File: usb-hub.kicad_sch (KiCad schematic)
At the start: 17 parts, among them U5 CH334P, Y2 X322512MSB4SI

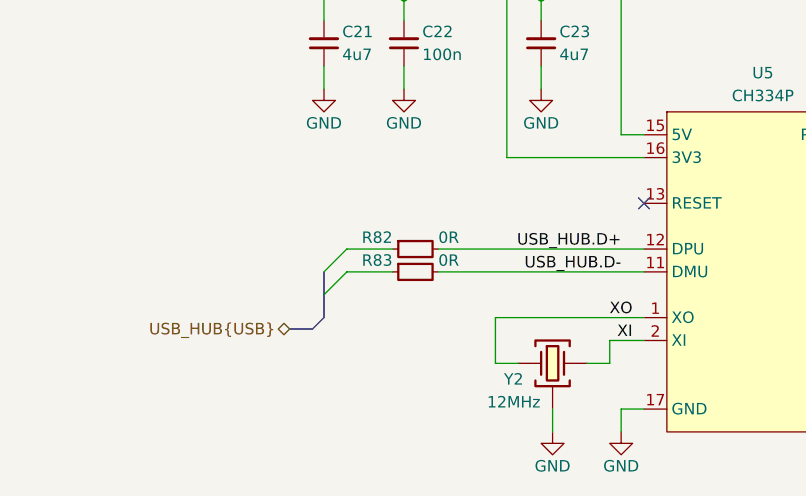
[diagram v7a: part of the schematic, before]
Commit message: [#3] Continue layout, minor schematic fixes, add power switch for CAN transceiver 5V rail
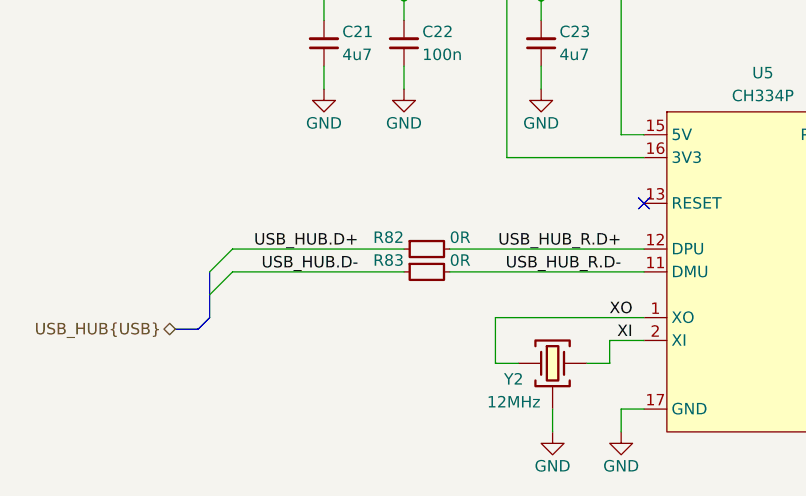
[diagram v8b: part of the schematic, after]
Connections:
- net USB_HUB.D+: now also R82.1; no longer R82.2, U5.12 (DPU)
- net USB_HUB.D-: now also R83.1; no longer R83.2, U5.11 (DMU)
- new net USB_HUB_R.D+: R82.2, U5.12 (DPU)
- new net USB_HUB_R.D-: R83.2, U5.11 (DMU)
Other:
- moved on the sheet: R82, R83
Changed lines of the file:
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@@
 	)
 	(bus_entry
-		(at 96.52 107.95)
+		(at 83.82 107.95)
 		(size 2.54 -2.54)
 		(stroke
@@
 	)
 	(bus_entry
-		(at 96.52 110.49)
+		(at 83.82 110.49)
 		(size 2.54 -2.54)
 		(stroke
@@
 	(bus
 		(pts
-			(xy 95.25 114.3) (xy 92.71 114.3)
+			(xy 82.55 114.3) (xy 80.01 114.3)
 		)
 		(stroke
@@
 	(wire
 		(pts
-			(xy 104.14 107.95) (xy 99.06 107.95)
+			(xy 105.41 107.95) (xy 86.36 107.95)
 		)
 		(stroke
@@
 	(wire
 		(pts
-			(xy 104.14 105.41) (xy 99.06 105.41)
+			(xy 105.41 105.41) (xy 86.36 105.41)
 		)
 		(stroke
@@
 	(bus
 		(pts
-			(xy 96.52 107.95) (xy 96.52 110.49)
+			(xy 83.82 107.95) (xy 83.82 110.49)
 		)
 		(stroke
@@
 	(bus
 		(pts
-			(xy 95.25 114.3) (xy 96.52 113.03)
+			(xy 82.55 114.3) (xy 83.82 113.03)
 		)
 		(stroke
@@
 	(bus
 		(pts
-			(xy 96.52 110.49) (xy 96.52 113.03)
+			(xy 83.82 110.49) (xy 83.82 113.03)
 		)
 		(stroke
@@
 	(wire
 		(pts
-			(xy 109.22 105.41) (xy 132.08 105.41)
+			(xy 110.49 105.41) (xy 132.08 105.41)
 		)
 		(stroke
@@
 	(wire
 		(pts
-			(xy 109.22 107.95) (xy 132.08 107.95)
+			(xy 110.49 107.95) (xy 132.08 107.95)
 		)
 		(stroke
@@
 		)
 	)
-	(label "USB_HUB.D-"
+	(label "USB_HUB_R.D-"
 		(at 129.54 107.95 180)
 		(effects
@@
 	)
 	(label "USB_HUB.D+"
+		(at 100.33 105.41 180)
+		(effects
+			(font
+				(size 1.27 1.27)
+			)
+			(justify right bottom)
+		)
+	)
+	(label "USB_HUB_R.D+"
 		(at 129.54 105.41 180)
 		(effects
@@
 		)
 	)
+	(label "USB_HUB.D-"
+		(at 100.33 107.95 180)
+		(effects
+			(font
+				(size 1.27 1.27)
+			)
+			(justify right bottom)
+		)
+	)
 	(label "USB_3_R.D+"
 		(at 161.29 113.03 0)
@@
 	(hierarchical_label "USB_HUB{USB}"
 		(shape bidirectional)
-		(at 92.71 114.3 180)
+		(at 80.01 114.3 180)
 		(effects
 			(font
@@
 		(polyline
 			(pts
-				(xy 93.98 110.49) (xy 130.81 110.49) (xy 130.81 101.6) (xy 93.98 101.6)
+				(xy 81.28 110.49) (xy 130.81 110.49) (xy 130.81 101.6) (xy 81.28 101.6)
 			)
 			(stroke
@@
 		(length 2.54)
 		(shape round)
-		(at 93.98 101.6 0)
+		(at 81.28 101.6 0)
 		(effects
 			(font
@@
 		)
 		(property "Netclass" "USB_90Ohm_diff"
-			(at 94.742 99.06 0)
+			(at 82.042 99.06 0)
 			(effects
 				(font
@@
 		)
 		(property "Component Class" ""
-			(at -133.35 -59.69 0)
+			(at -146.05 -59.69 0)
 			(effects
 				(font
@@
 	(symbol
 		(lib_id "DW-resistors:R-0R-0402")
-		(at 104.14 107.95 0)
+		(at 105.41 107.95 0)
 		(unit 1)
 		(exclude_from_sim no)
@@
 		(dnp no)
 		(property "Reference" "R83"
-			(at 104.14 106.68 0)
+			(at 105.41 106.68 0)
 			(effects
 				(font
@@
 		)
 		(property "Value" "R-0R-0402"
-			(at 116.84 110.49 0)
+			(at 118.11 110.49 0)
 			(effects
 				(font
@@
 		)
 		(property "Footprint" "DW-footprints:R_0402_1005Metric"
-			(at 116.84 113.03 0)
+			(at 118.11 113.03 0)
 			(effects
 				(font
@@
 		)
 		(property "Datasheet" "https://lcsc.com/datasheet/lcsc_datasheet_2411221126_UNI-ROYAL-0402WGF0000TCE_C17168.pdf"
-			(at 116.84 115.57 0)
+			(at 118.11 115.57 0)
 			(effects
 				(font
@@
 		)
 		(property "Description" "62.5mW Thick Film Resistor 50V ±800ppm/℃ ±1% 0Ω 0402 Chip Resistor - Surface Mount ROHS"
-			(at 116.84 118.11 0)
+			(at 118.11 118.11 0)
 			(effects
 				(font
@@
 		)
 		(property "Manufacturer" "UNI-ROYAL(Uniroyal Elec)"
-			(at 116.84 120.65 0)
+			(at 118.11 120.65 0)
 			(effects
 				(font
@@
 		)
 		(property "MPN" "0402WGF0000TCE"
-			(at 116.84 123.19 0)
+			(at 118.11 123.19 0)
 			(effects
 				(font
@@
 		)
 		(property "LCSC" "C17168"
-			(at 116.84 125.73 0)
+			(at 118.11 125.73 0)
 			(effects
 				(font
@@
 		)
 		(property "Val" "0R"
-			(at 109.22 106.68 0)
+			(at 110.49 106.68 0)
 			(effects
 				(font
@@
 		)
 		(property "Tolerance" "1%"
-			(at 116.84 130.81 0)
+			(at 118.11 130.81 0)
 			(effects
 				(font
@@
 	(symbol
 		(lib_id "DW-resistors:R-0R-0402")
-		(at 104.14 105.41 0)
+		(at 105.41 105.41 0)
 		(unit 1)
 		(exclude_from_sim no)
@@
 		(dnp no)
 		(property "Reference" "R82"
-			(at 104.14 104.14 0)
+			(at 105.41 104.14 0)
 			(effects
 				(font
@@
 		)
 		(property "Value" "R-0R-0402"
-			(at 116.84 107.95 0)
+			(at 118.11 107.95 0)
 			(effects
 				(font
@@
 		)
 		(property "Footprint" "DW-footprints:R_0402_1005Metric"
-			(at 116.84 110.49 0)
+			(at 118.11 110.49 0)
 			(effects
 				(font
@@
 		)
 		(property "Datasheet" "https://lcsc.com/datasheet/lcsc_datasheet_2411221126_UNI-ROYAL-0402WGF0000TCE_C17168.pdf"
-			(at 116.84 113.03 0)
+			(at 118.11 113.03 0)
 			(effects
 				(font
@@
 		)
 		(property "Description" "62.5mW Thick Film Resistor 50V ±800ppm/℃ ±1% 0Ω 0402 Chip Resistor - Surface Mount ROHS"
-			(at 116.84 115.57 0)
+			(at 118.11 115.57 0)
 			(effects
 				(font
@@
 		)
 		(property "Manufacturer" "UNI-ROYAL(Uniroyal Elec)"
-			(at 116.84 118.11 0)
+			(at 118.11 118.11 0)
 			(effects
 				(font
@@
 		)
 		(property "MPN" "0402WGF0000TCE"
-			(at 116.84 120.65 0)
+			(at 118.11 120.65 0)
 			(effects
 				(font
@@
 		)
 		(property "LCSC" "C17168"
-			(at 116.84 123.19 0)
+			(at 118.11 123.19 0)
 			(effects
 				(font
@@
 		)
 		(property "Val" "0R"
-			(at 109.22 104.14 0)
+			(at 110.49 104.14 0)
 			(effects
 				(font
@@
 		)
 		(property "Tolerance" "1%"
-			(at 116.84 128.27 0)
+			(at 118.11 128.27 0)
 			(effects
 				(font
